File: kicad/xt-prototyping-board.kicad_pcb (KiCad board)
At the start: 2 copper layers, 194.3 x 93.3 mm, 58 parts

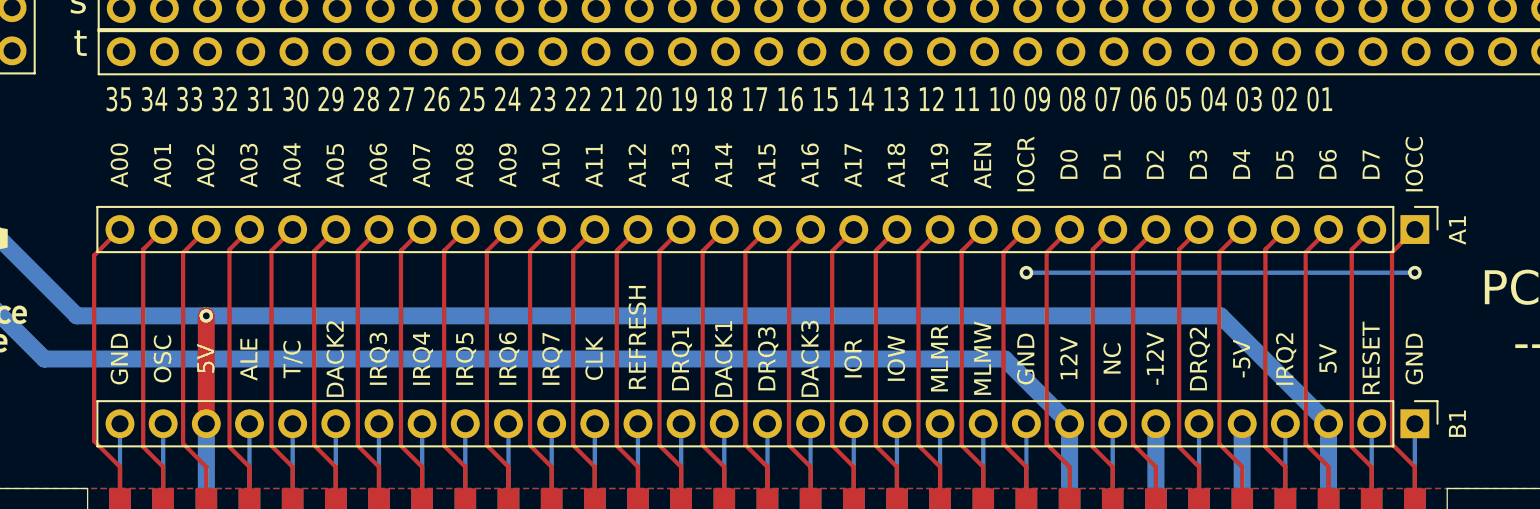
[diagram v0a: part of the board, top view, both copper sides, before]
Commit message: Add isa pin id text on the back
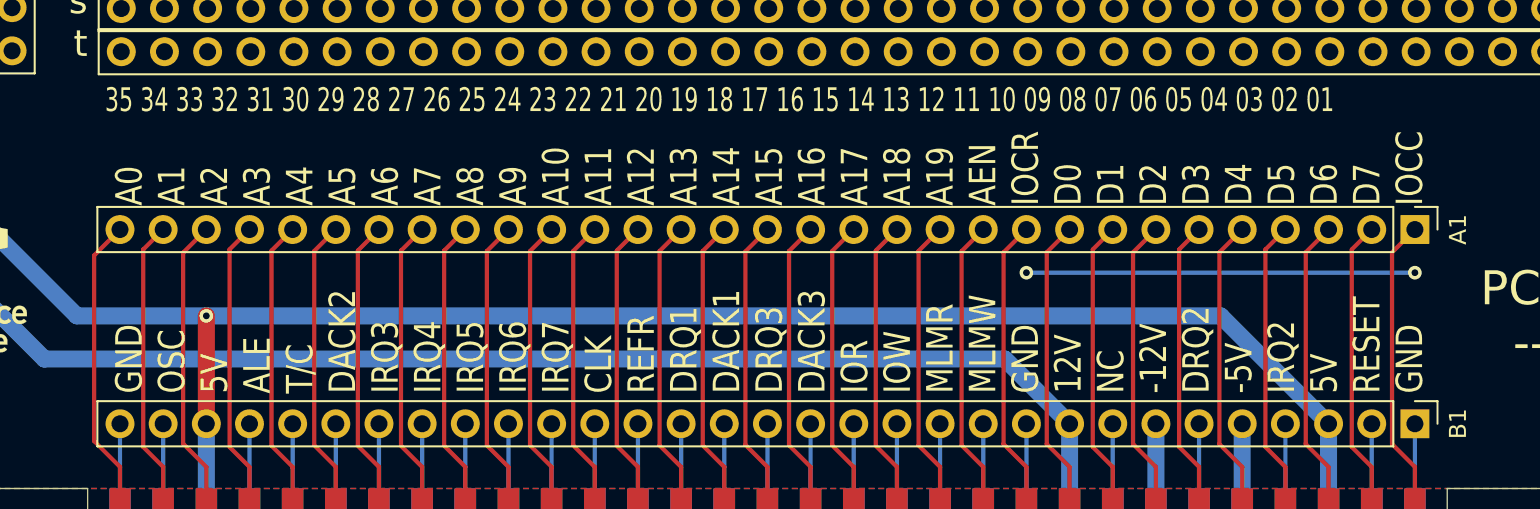
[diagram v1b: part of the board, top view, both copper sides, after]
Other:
- board text added: "A0 A1 A2 A3 A4 A5 A6 A7 A8 A9 A10 A11 A12 A13 A14 A15 A16 A17 A18 A19 AEN IOCR D0 D1 D2 D3 D4 D5 D6 D7 IOCC"
- board text added: "GND OSC 5V ALE T/C DACK2 IRQ3 IRQ4 IRQ5 IRQ6 IRQ7 CLK REFR DRQ1 DACK1 DRQ3 DACK3 IOR IOW MLMR MLMW GND 12V NC -12V DRQ2 -5V IRQ2 5V RESET GND"

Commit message: Minor silk layer fixes
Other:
- board text added: "PC Back ---->"
- board text added: "PC Back <----"
- board text removed: "PC Back ----->"
- board text removed: "PC Back <-----"

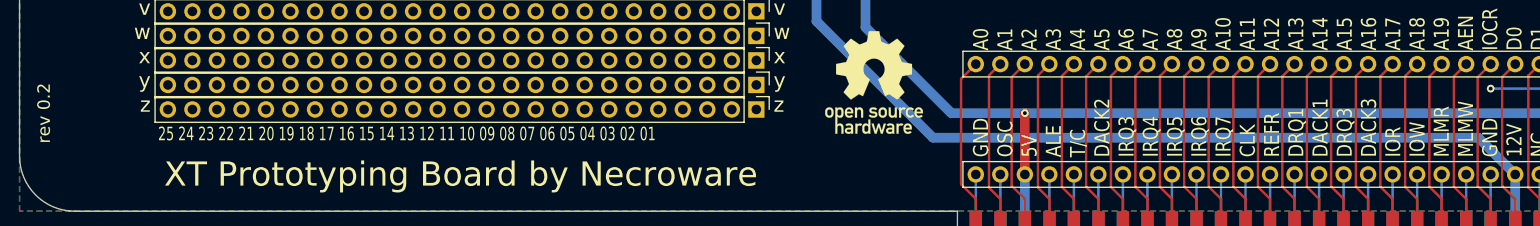
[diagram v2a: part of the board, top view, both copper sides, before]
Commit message: Fix silk layer, now proper low active symbols
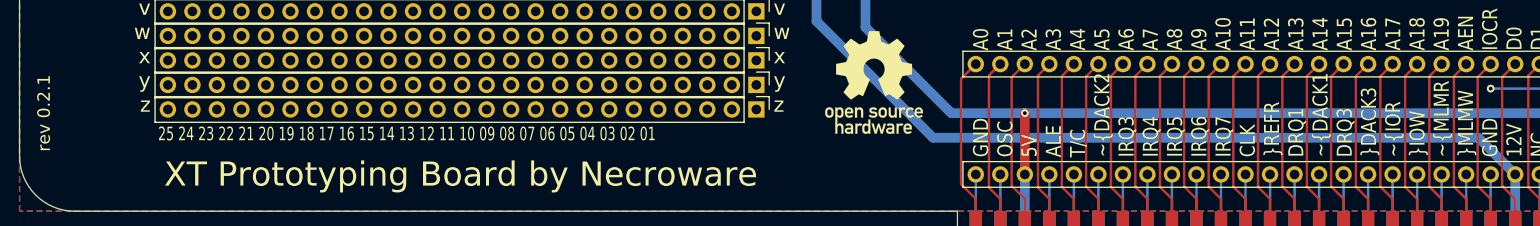
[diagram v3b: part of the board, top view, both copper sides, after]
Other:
- board text added: "GND OSC 5V ALE T/C ~DACK2 IRQ3 IRQ4 IRQ5 IRQ6 IRQ7 CLK ~REFR DRQ1 ~DACK1 DRQ3 ~DACK3 ~IOR ~IOW ~MLMR ~MLMW GND 12V NC -12V DRQ2 -5V IRQ2 5V RESET GND"
- board text added: "rev 0.2.1"
- board text removed: "GND OSC 5V ALE T/C DACK2 IRQ3 IRQ4 IRQ5 IRQ6 IRQ7 CLK REFR DRQ1 DACK1 DRQ3 DACK3 IOR IOW MLMR MLMW GND 12V NC -12V DRQ2 -5V IRQ2 5V RESET GND"
- board text removed: "rev 0.2"

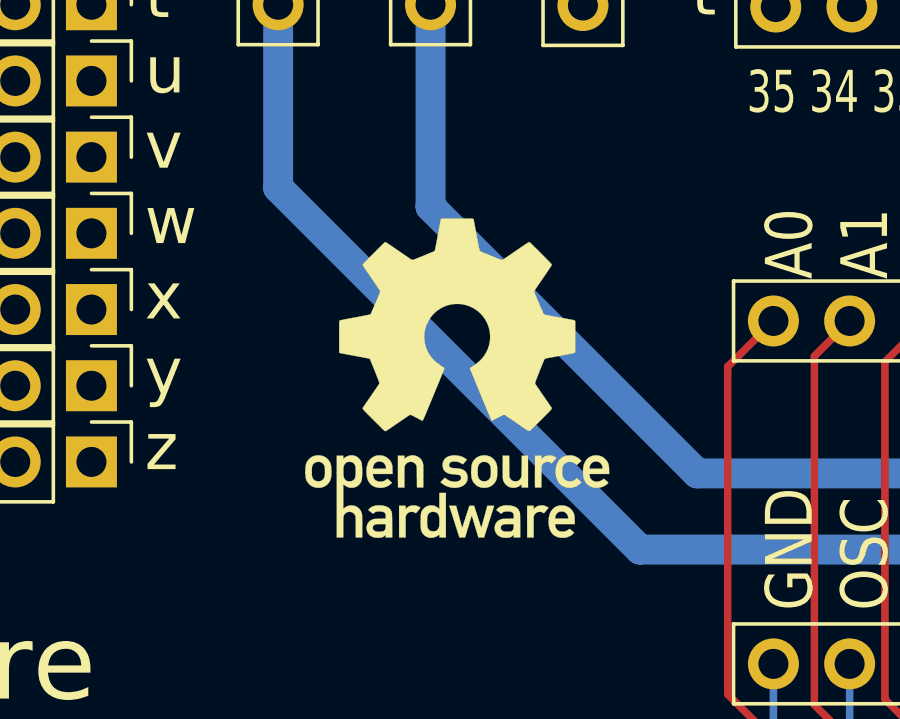
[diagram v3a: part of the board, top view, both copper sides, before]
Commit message: Take OSHW Icon from Kicad std lib
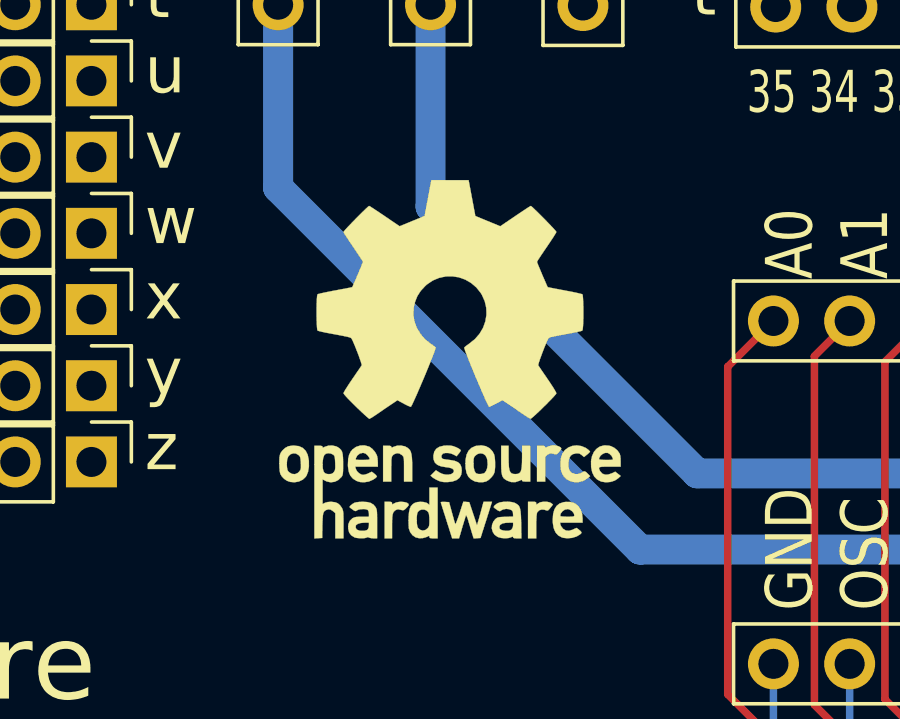
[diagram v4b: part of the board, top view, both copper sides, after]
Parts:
- removed G***: LOGO, necroware:open_hardware_logo
- added REF**: OSHW-Logo_11.4x12mm_SilkScreen, Symbol:OSHW-Logo_11.4x12mm_SilkScreen, F.Cu at (132.7, 132.1)
